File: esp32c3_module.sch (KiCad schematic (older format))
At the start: 17 parts, among them J1 Conn_01x15_Male, J2 Conn_01x15_Male, Q1 S8050, Q2 S8050, SW1 BOOT, SW2 RST, U3 ESP32-C3-WROOM-02

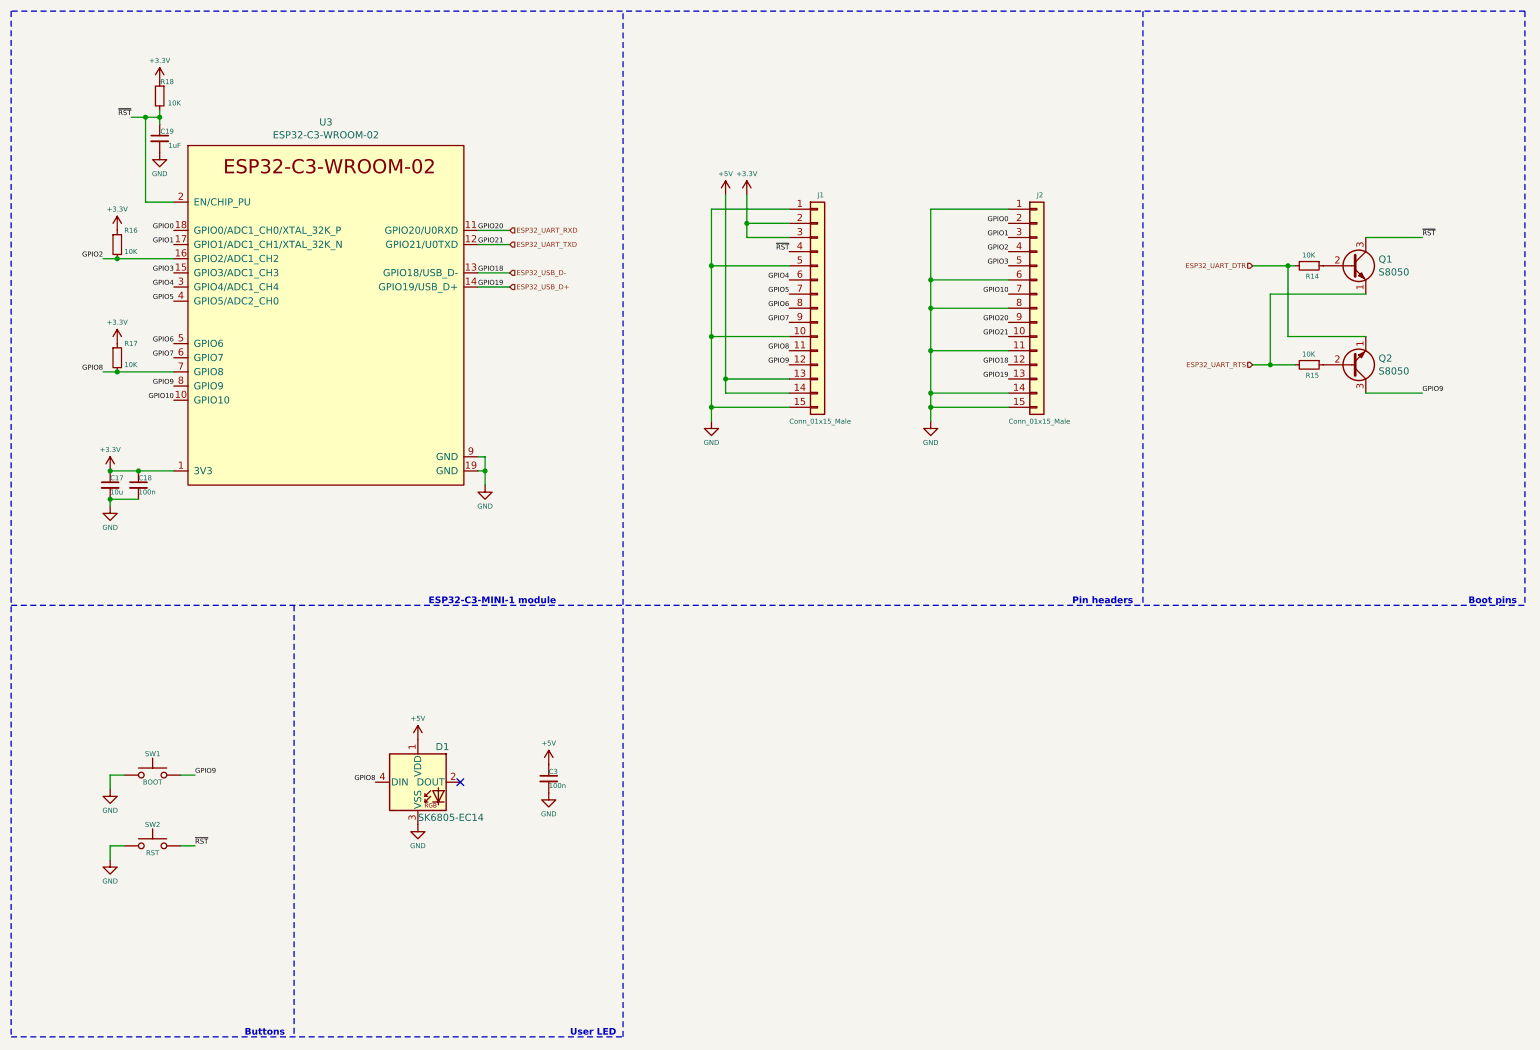
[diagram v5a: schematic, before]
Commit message: PCB: Rough component placement done
Signed-off-by: Tomislav Milkovic <tomislav.milkovic95@gmail.com>
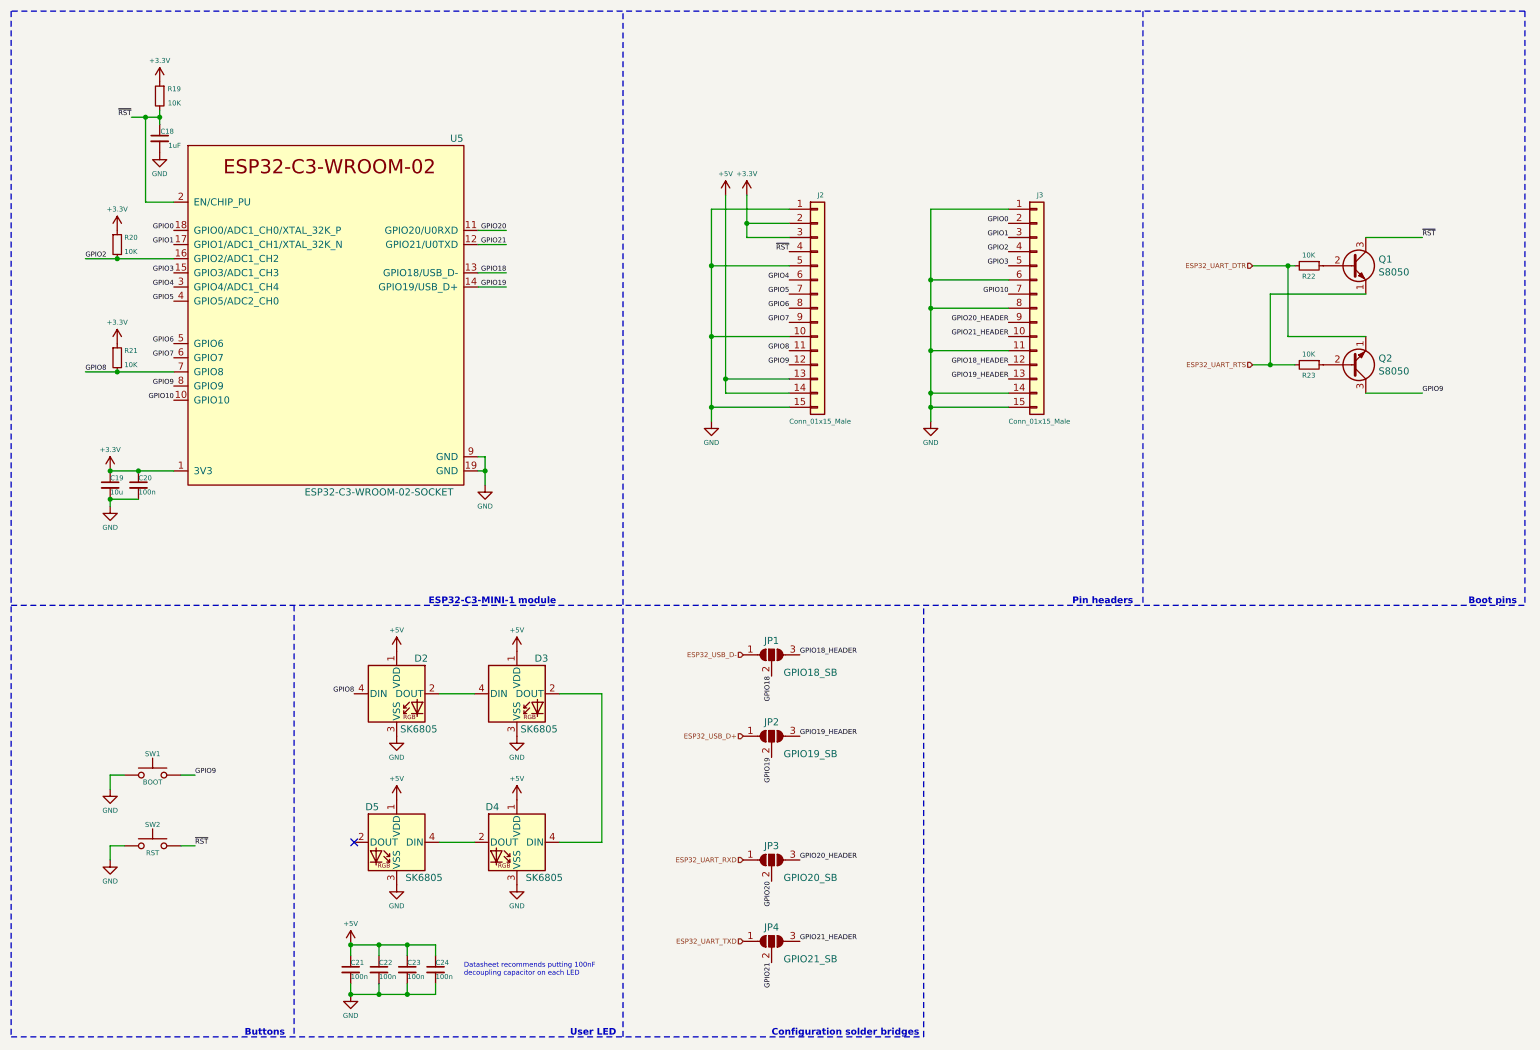
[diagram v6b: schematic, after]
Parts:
- added C22, C23, C24: 100n, Capacitor_SMD:C_0402_1005Metric, symbol Device:C_Small
- added D3, D4, D5: SK6805, LED_custom:LED_SK6805_E14_1.4x1.4mm_P0.4mm, symbol LED:WS2812B
- added JP1: GPIO18_SB, Jumper:SolderJumper-3_P1.3mm_Open_RoundedPad1.0x1.5mm, symbol Jumper:SolderJumper_3_Open
- added JP2: GPIO19_SB, Jumper:SolderJumper-3_P1.3mm_Open_RoundedPad1.0x1.5mm, symbol Jumper:SolderJumper_3_Open
- added JP3: GPIO20_SB, Jumper:SolderJumper-3_P1.3mm_Open_RoundedPad1.0x1.5mm, symbol Jumper:SolderJumper_3_Open
- added JP4: GPIO21_SB, Jumper:SolderJumper-3_P1.3mm_Open_RoundedPad1.0x1.5mm, symbol Jumper:SolderJumper_3_Open
- D2: renamed from D1; value SK6805-EC14 -> SK6805
- U5: renamed from U3; value ESP32-C3-WROOM-02 -> ESP32-C3-WROOM-02-SOCKET
- renumbered C19 to C18, C17 to C19, C18 to C20, C3 to C21, J1 to J2, J2 to J3, R18 to R19, R16 to R20, R17 to R21, R14 to R22, R15 to R23
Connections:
- net +5V: now also C22.1, C23.1, C24.1, D3.1 (VDD), D4.1 (VDD), D5.1 (VDD)
- net ESP32_UART_RXD: now also JP3.1 (A); no longer J3.9 (Pin_9), U5.11 (GPIO20/U0RXD)
- net ESP32_UART_TXD: now also JP4.1 (A); no longer J3.10 (Pin_10), U5.12 (GPIO21/U0TXD)
- net ESP32_USB_D+: now also JP2.1 (A); no longer J3.13 (Pin_13), U5.14 (GPIO19/USB_D+)
- net ESP32_USB_D-: now also JP1.1 (A); no longer J3.12 (Pin_12), U5.13 (GPIO18/USB_D-)
- net GND: now also C22.2, C23.2, C24.2, D3.3 (VSS), D4.3 (VSS), D5.3 (VSS)
- net at D2.2 (DOUT): now also D3.4 (DIN)
- new net: D3.2 (DOUT), D4.4 (DIN)
- new net: D4.2 (DOUT), D5.4 (DIN)
- new net GPIO18: JP1.2 (C), U5.13 (GPIO18/USB_D-)
- new net GPIO18_HEADER: J3.12 (Pin_12), JP1.3 (B)
- new net GPIO19: JP2.2 (C), U5.14 (GPIO19/USB_D+)
- new net GPIO19_HEADER: J3.13 (Pin_13), JP2.3 (B)
- new net GPIO20: JP3.2 (C), U5.11 (GPIO20/U0RXD)
- new net GPIO20_HEADER: J3.9 (Pin_9), JP3.3 (B)
- new net GPIO21: JP4.2 (C), U5.12 (GPIO21/U0TXD)
- new net GPIO21_HEADER: J3.10 (Pin_10), JP4.3 (B)
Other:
- note added: "Configuration solder bridges"
- note added: "Datasheet recommends putting 100nF\ndecoupling capacitor on each LED"
- moved on the sheet: C21, D2

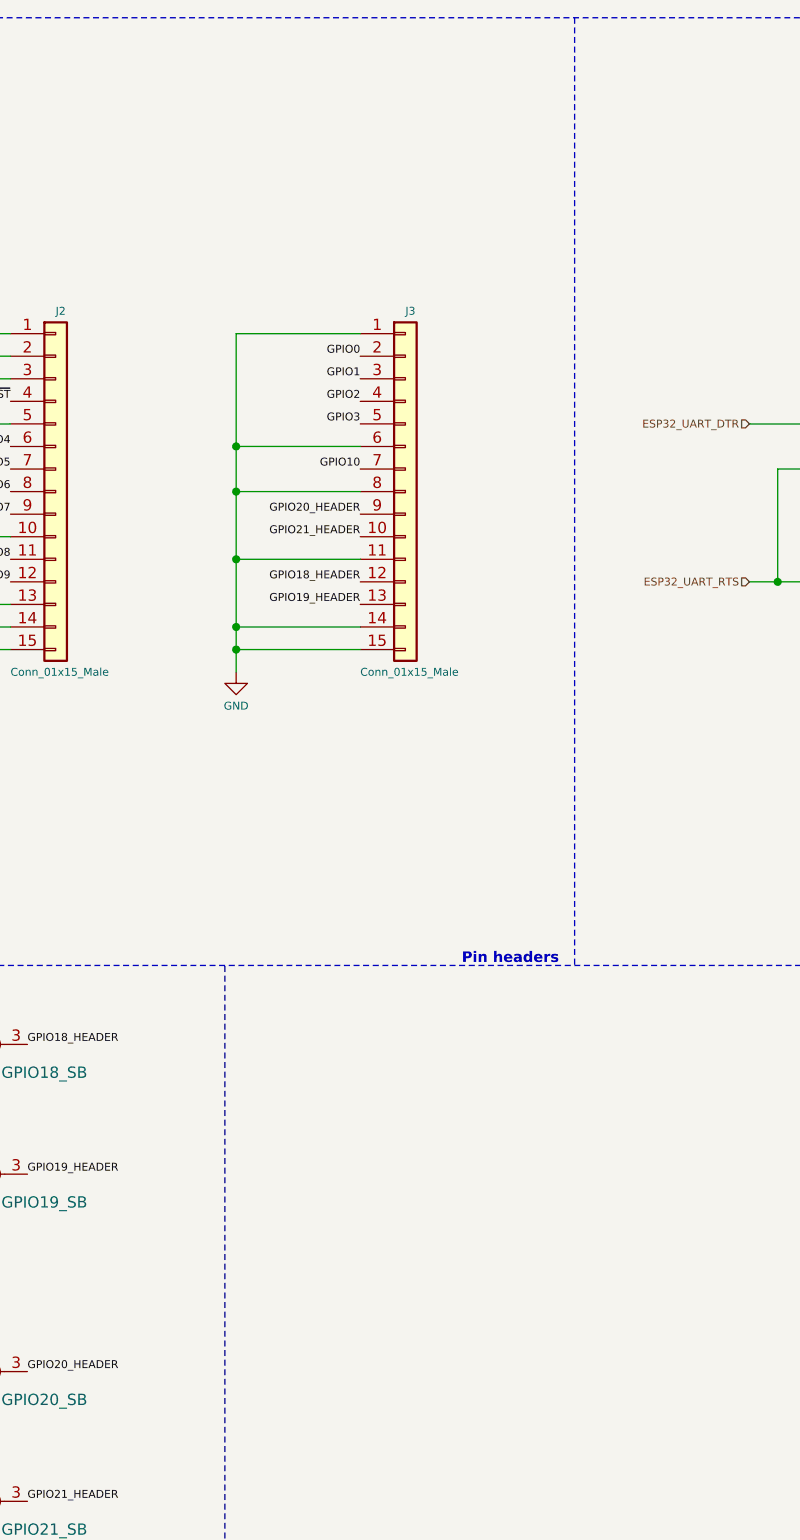
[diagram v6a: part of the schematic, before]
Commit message: Add fiducials, finish routing
Signed-off-by: Tomislav Milkovic <tomislav.milkovic95@gmail.com>
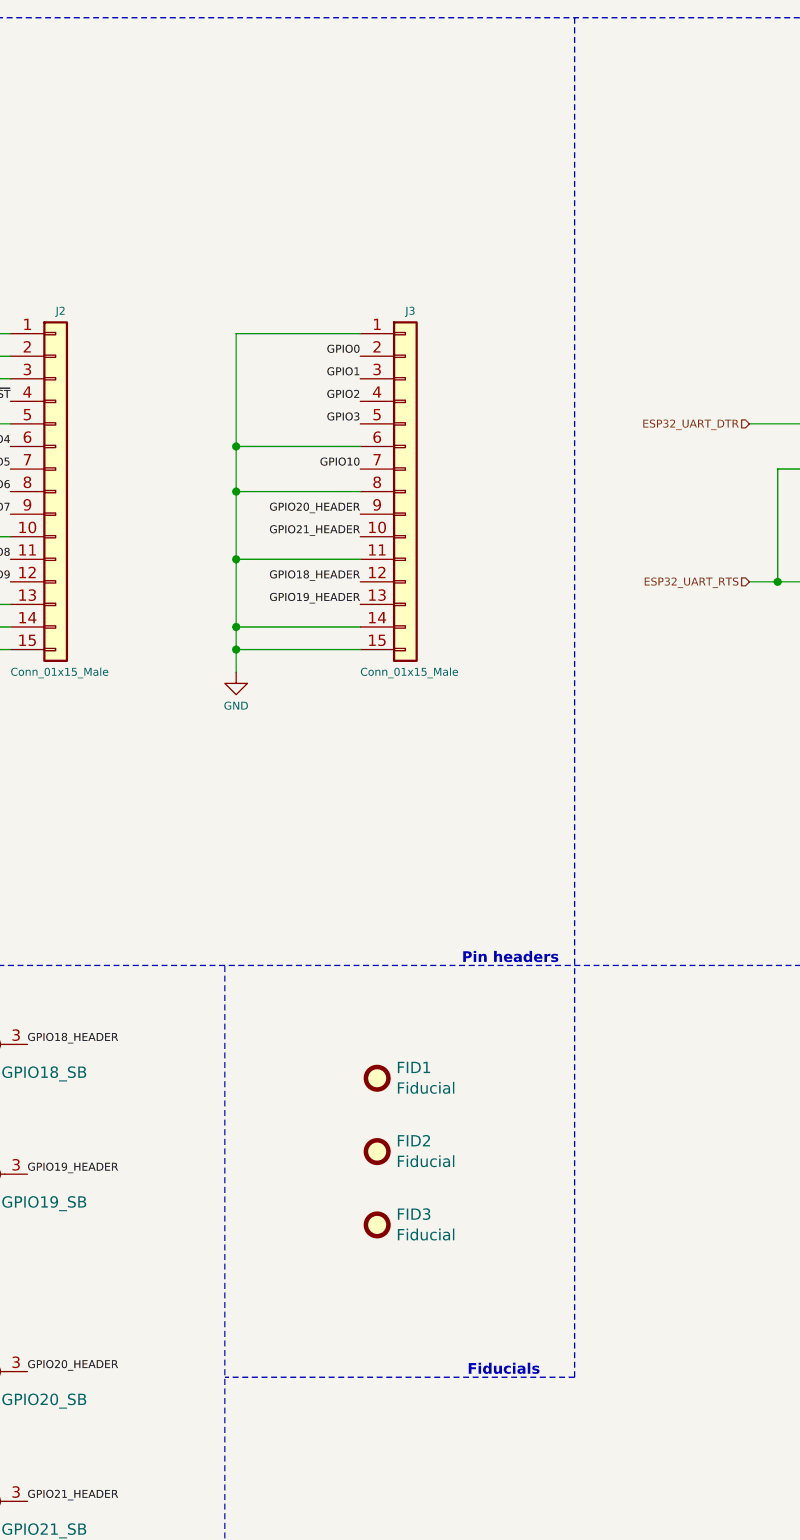
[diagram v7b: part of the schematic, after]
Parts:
- added FID1, FID2, FID3: Fiducial, Fiducial:Fiducial_0.5mm_Mask1mm, symbol Mechanical:Fiducial
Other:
- note added: "Fiducials"
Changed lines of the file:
@@
 	500  500  500  7750
-Wire Notes Line
-	8500 500  8500 4700
 Wire Notes Line
 	11200 500  11200 4700
@@
 Wire Wire Line
 	3800 2150 4000 2150
+$Comp
+L Mechanical:Fiducial FID1
+U 1 1 67BA2381
+P 7625 5200
+F 0 "FID1" H 7710 5246 50  0000 L CNN
+F 1 "Fiducial" H 7710 5155 50  0000 L CNN
+F 2 "Fiducial:Fiducial_0.5mm_Mask1mm" H 7625 5200 50  0001 C CNN
+F 3 "~" H 7625 5200 50  0001 C CNN
+	1    7625 5200
+	1    0    0    -1
+$EndComp
+$Comp
+L Mechanical:Fiducial FID2
+U 1 1 67BA358A
+P 7625 5525
+F 0 "FID2" H 7710 5571 50  0000 L CNN
+F 1 "Fiducial" H 7710 5480 50  0000 L CNN
+F 2 "Fiducial:Fiducial_0.5mm_Mask1mm" H 7625 5525 50  0001 C CNN
+F 3 "~" H 7625 5525 50  0001 C CNN
+	1    7625 5525
+	1    0    0    -1
+$EndComp
+$Comp
+L Mechanical:Fiducial FID3
+U 1 1 67BA4000
+P 7625 5850
+F 0 "FID3" H 7710 5896 50  0000 L CNN
+F 1 "Fiducial" H 7710 5805 50  0000 L CNN
+F 2 "Fiducial:Fiducial_0.5mm_Mask1mm" H 7625 5850 50  0001 C CNN
+F 3 "~" H 7625 5850 50  0001 C CNN
+	1    7625 5850
+	1    0    0    -1
+$EndComp
+Wire Notes Line
+	8500 6525 6950 6525
+Wire Notes Line
+	8500 500  8500 6525
+Text Notes 8025 6525 0    47   ~ 9
+Fiducials
 $EndSCHEMATC
